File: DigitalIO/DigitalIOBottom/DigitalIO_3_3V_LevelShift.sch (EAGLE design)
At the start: 72 parts, among them IC1 MCP23017SP, IC2 ULN2803A, K5 HF46105, K6 HF46105, K7 HF46105, K8 HF46105, P1 DF11-06-2DSA, Q1 BS170, Q2 BS170, Q5 691131710002, Q6 691131710002, Q7 691131710002, Q8 691131710002, X1 691131710005, X2 691131710004

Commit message: Changed some drills, pads, holes, routes and headers.
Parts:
- removed X3: (no value), pinhead:PINHD-1X5
- added 5V, PQ1, PQ2, PQ3, PQ4: WIREPAD1,6/0,8, wirepad:WIREPAD1,6/0,8
- P1: value DF11-06-2DSA -> DF11-06-2DS; device con-hirose-df11:DF11-06-2DSA -> con-hirose-df11:DF11-06-2DS
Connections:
- net +5V: now also 5V.P; no longer X3.1
- net N$28: now also PQ4.P; no longer X3.5
- net N$30: now also PQ3.P; no longer X3.4
- net N$32: now also PQ2.P; no longer X3.3
- net N$34: now also PQ1.P; no longer X3.2

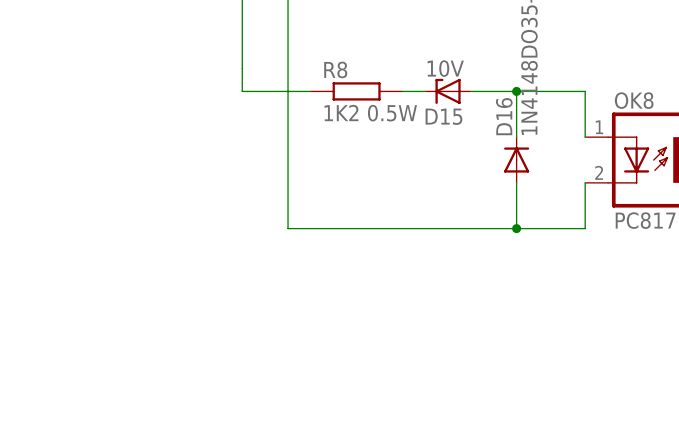
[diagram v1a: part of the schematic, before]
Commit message: Add ground planes. Prepare for production.
Signed-off-by: Alexander Falkenstern <alexander.falkenstern@gmail.com>
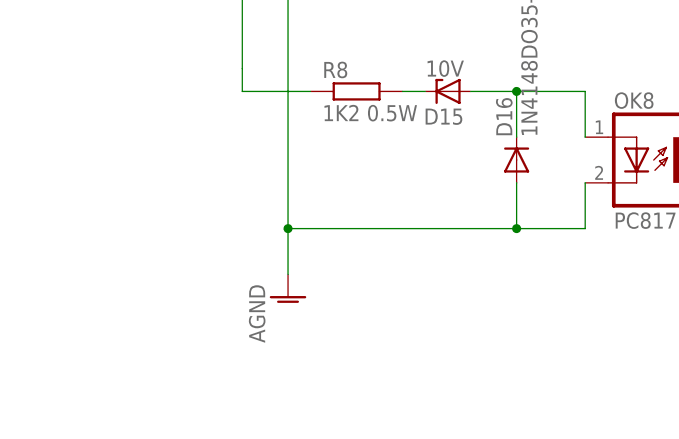
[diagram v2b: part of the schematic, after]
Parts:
- C1, C2: device capacitor-wima:C2,5-3 -> rcl:C-EUC0805
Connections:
- net N$11 renamed AGND

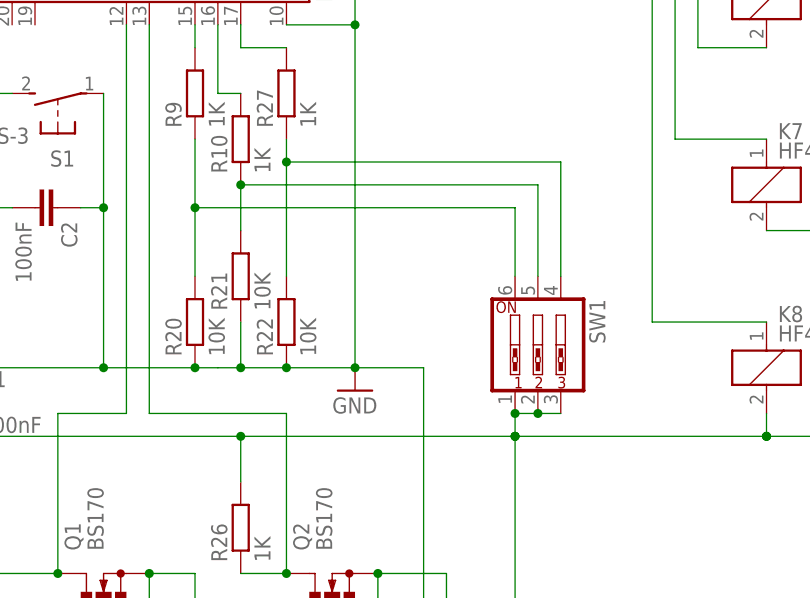
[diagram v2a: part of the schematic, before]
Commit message: Fix address selection. Increase some drills.
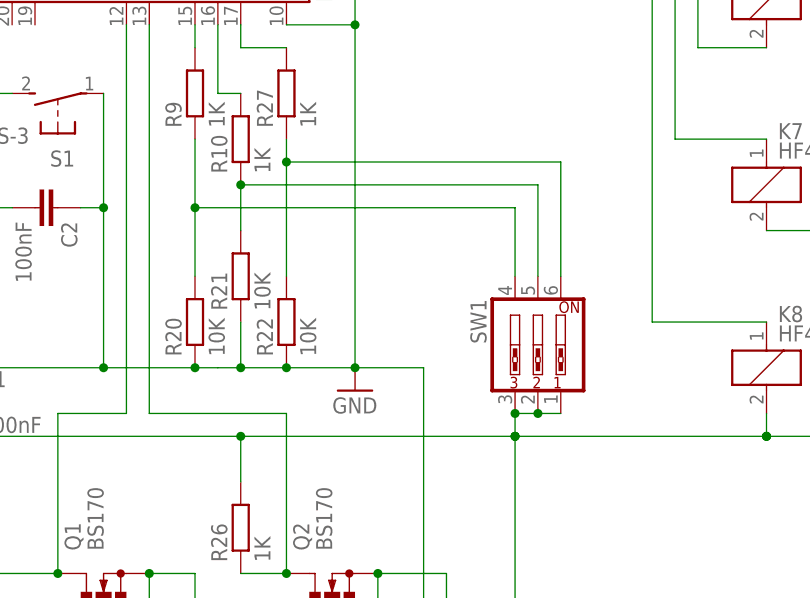
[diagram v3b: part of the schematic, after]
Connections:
- removed net N$36: R22.2, R27.1, SW1.4
- new net N$11: R22.2, R27.1, SW1.6
- net N$77: now also SW1.4; no longer SW1.6
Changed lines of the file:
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@@
 <attribute name="MPN" x="-335.28" y="83.82" size="1.778" layer="96" display="off"/>
 </instance>
-<instance part="SW1" gate="A" x="-271.78" y="76.2" rot="R270">
-<attribute name="OC_FARNELL" x="-271.78" y="76.2" size="1.778" layer="96" display="off"/>
-<attribute name="MF" x="-271.78" y="76.2" size="1.778" layer="96" display="off"/>
-<attribute name="MPN" x="-271.78" y="76.2" size="1.778" layer="96" display="off"/>
+<instance part="SW1" gate="A" x="-271.78" y="76.2" rot="MR270">
+<attribute name="OC_FARNELL" x="-271.78" y="76.2" size="1.778" layer="96" rot="MR0" display="off"/>
+<attribute name="MF" x="-271.78" y="76.2" size="1.778" layer="96" rot="MR0" display="off"/>
+<attribute name="MPN" x="-271.78" y="76.2" size="1.778" layer="96" rot="MR0" display="off"/>
 </instance>
 <instance part="R20" gate="G$1" x="-309.88" y="78.74" rot="R90">
@@
 <junction x="-233.68" y="88.9"/>
 <pinref part="IC1" gate="G$1" pin="VDD"/>
-<pinref part="SW1" gate="A" pin="1"/>
-<pinref part="SW1" gate="A" pin="2"/>
-<pinref part="SW1" gate="A" pin="3"/>
 <wire x1="-340.36" y1="66.04" x2="-340.36" y2="78.74" width="0.1524" layer="91"/>
 <wire x1="-340.36" y1="78.74" x2="-340.36" y2="111.76" width="0.1524" layer="91"/>
-<wire x1="-271.78" y1="68.58" x2="-269.24" y2="68.58" width="0.1524" layer="91"/>
 <pinref part="OK8" gate="A" pin="COL"/>
-<wire x1="-271.78" y1="68.58" x2="-274.32" y2="68.58" width="0.1524" layer="91"/>
 <wire x1="-383.54" y1="43.18" x2="-370.84" y2="43.18" width="0.1524" layer="91"/>
 <wire x1="-370.84" y1="43.18" x2="-370.84" y2="66.04" width="0.1524" layer="91"/>
@@
 <junction x="-340.36" y="78.74"/>
 <wire x1="-274.32" y1="66.04" x2="-304.8" y2="66.04" width="0.1524" layer="91"/>
-<junction x="-274.32" y="68.58"/>
-<wire x1="-274.32" y1="68.58" x2="-274.32" y2="66.04" width="0.1524" layer="91"/>
-<junction x="-271.78" y="68.58"/>
 <wire x1="-340.36" y1="66.04" x2="-335.28" y2="66.04" width="0.1524" layer="91"/>
 <wire x1="-335.28" y1="66.04" x2="-304.8" y2="66.04" width="0.1524" layer="91"/>
@@
 <pinref part="5V" gate="G$1" pin="P"/>
 <junction x="-233.68" y="175.26"/>
+<pinref part="SW1" gate="A" pin="1"/>
+<pinref part="SW1" gate="A" pin="3"/>
+<pinref part="SW1" gate="A" pin="2"/>
+<wire x1="-271.78" y1="68.58" x2="-274.32" y2="68.58" width="0.1524" layer="91"/>
+<junction x="-271.78" y="68.58"/>
+<wire x1="-271.78" y1="68.58" x2="-269.24" y2="68.58" width="0.1524" layer="91"/>
+<wire x1="-274.32" y1="66.04" x2="-274.32" y2="68.58" width="0.1524" layer="91"/>
+<junction x="-274.32" y="68.58"/>
 </segment>
 </net>
@@
 <segment>
 <pinref part="R20" gate="G$1" pin="2"/>
-<wire x1="-309.88" y1="83.82" x2="-309.88" y2="91.44" width="0.1524" layer="91"/>
-<pinref part="SW1" gate="A" pin="6"/>
-<wire x1="-309.88" y1="91.44" x2="-274.32" y2="91.44" width="0.1524" layer="91"/>
-<wire x1="-274.32" y1="91.44" x2="-274.32" y2="83.82" width="0.1524" layer="91"/>
 <pinref part="R9" gate="G$1" pin="1"/>
 <wire x1="-309.88" y1="99.06" x2="-309.88" y2="91.44" width="0.1524" layer="91"/>
+<pinref part="SW1" gate="A" pin="4"/>
+<wire x1="-309.88" y1="91.44" x2="-309.88" y2="83.82" width="0.1524" layer="91"/>
+<wire x1="-274.32" y1="83.82" x2="-274.32" y2="91.44" width="0.1524" layer="91"/>
+<wire x1="-274.32" y1="91.44" x2="-309.88" y2="91.44" width="0.1524" layer="91"/>
 <junction x="-309.88" y="91.44"/>
 </segment>
@@
 <pinref part="R10" gate="G$1" pin="1"/>
 <junction x="-304.8" y="93.98"/>
-</segment>
-</net>
-<net name="N$36" class="0">
-<segment>
-<pinref part="R22" gate="G$1" pin="2"/>
-<wire x1="-299.72" y1="99.06" x2="-299.72" y2="96.52" width="0.1524" layer="91"/>
-<pinref part="R27" gate="G$1" pin="1"/>
-<pinref part="SW1" gate="A" pin="4"/>
-<wire x1="-299.72" y1="96.52" x2="-299.72" y2="83.82" width="0.1524" layer="91"/>
-<wire x1="-269.24" y1="96.52" x2="-269.24" y2="83.82" width="0.1524" layer="91"/>
-<wire x1="-299.72" y1="96.52" x2="-269.24" y2="96.52" width="0.1524" layer="91"/>
-<junction x="-299.72" y="96.52"/>
 </segment>
 </net>
@@
 </segment>
 </net>
+<net name="N$11" class="0">
+<segment>
+<pinref part="SW1" gate="A" pin="6"/>
+<wire x1="-269.24" y1="96.52" x2="-269.24" y2="83.82" width="0.1524" layer="91"/>
+<pinref part="R22" gate="G$1" pin="2"/>
+<pinref part="R27" gate="G$1" pin="1"/>
+<wire x1="-299.72" y1="99.06" x2="-299.72" y2="96.52" width="0.1524" layer="91"/>
+<wire x1="-299.72" y1="96.52" x2="-299.72" y2="83.82" width="0.1524" layer="91"/>
+<wire x1="-269.24" y1="96.52" x2="-299.72" y2="96.52" width="0.1524" layer="91"/>
+<junction x="-299.72" y="96.52"/>
+</segment>
+</net>

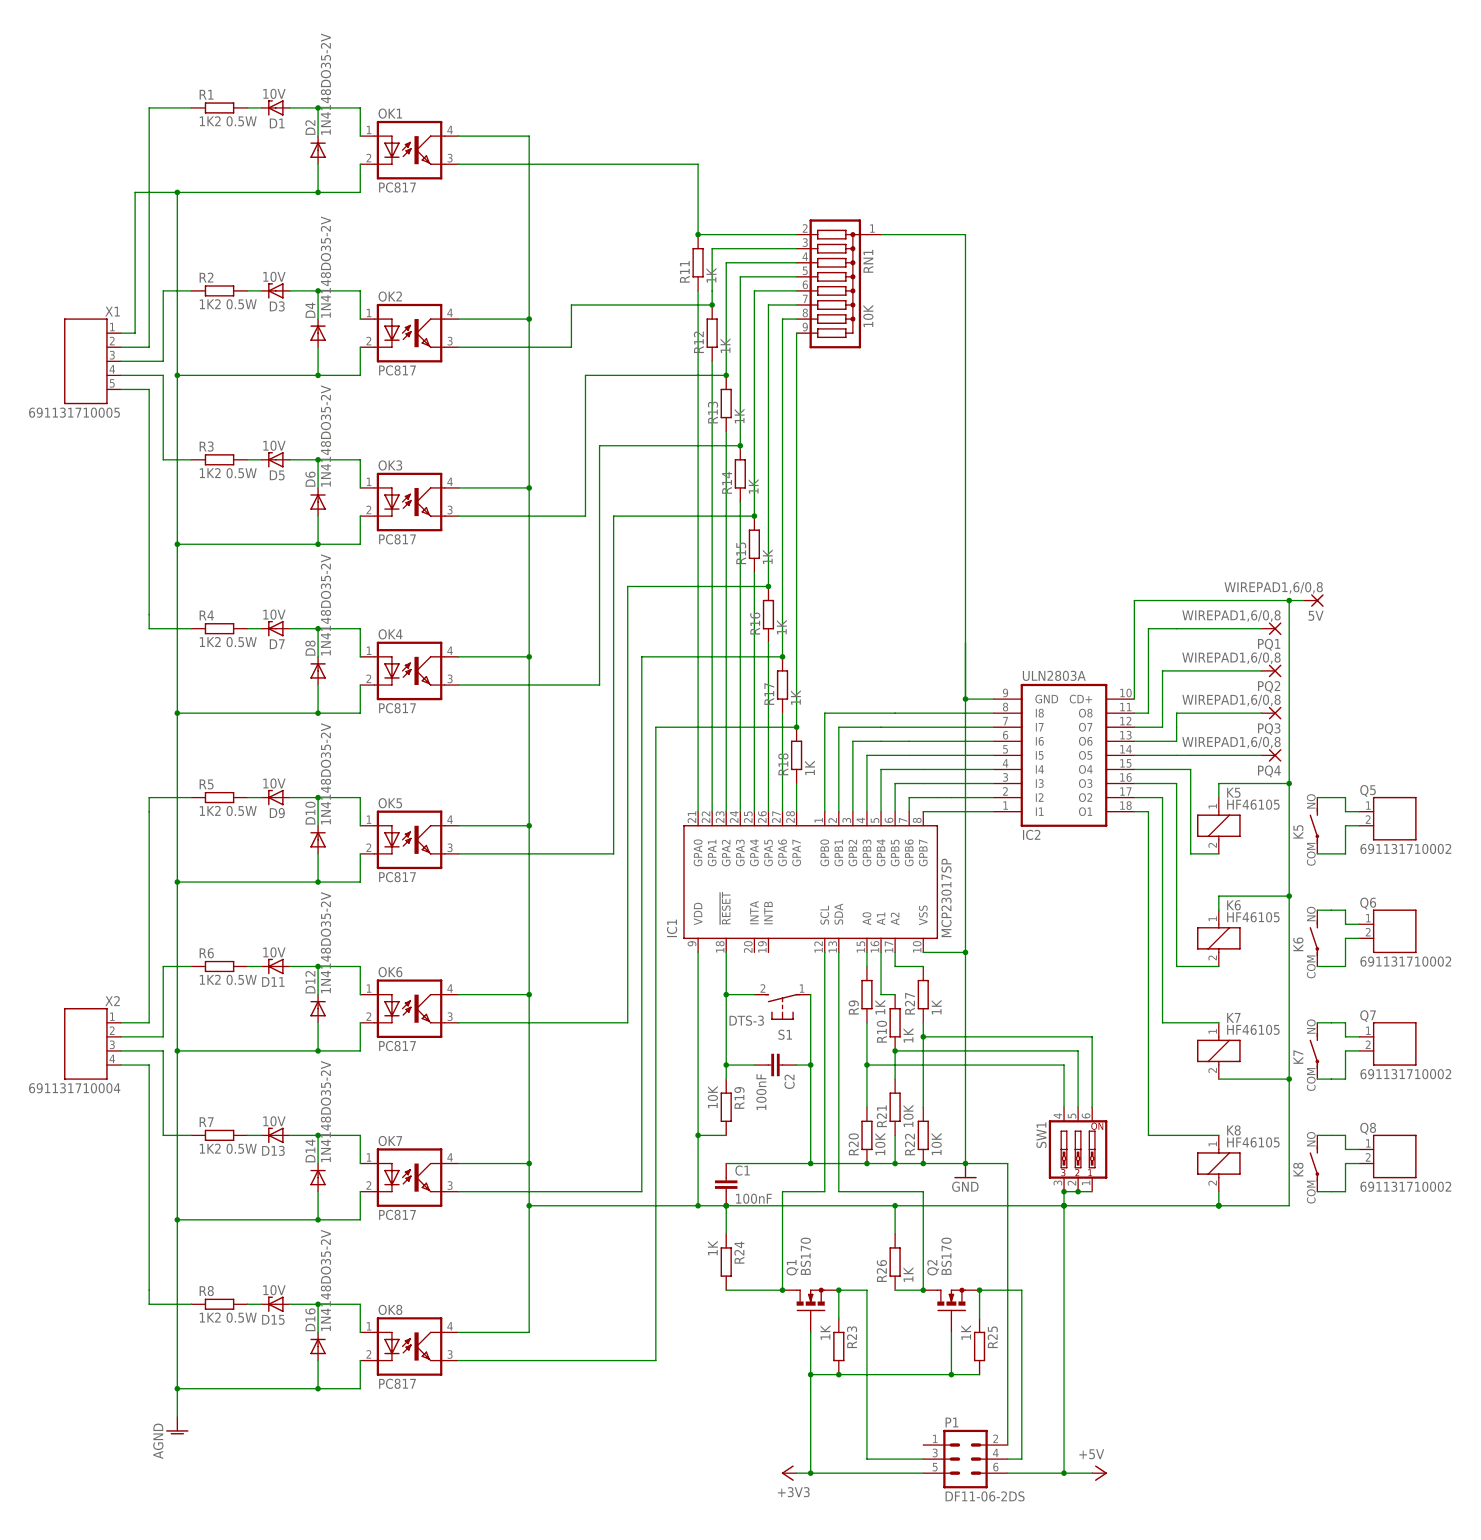
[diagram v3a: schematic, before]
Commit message: Add power switch and I2C interrupt wire. Add pull-up resistors for I2C. Adapt drills.
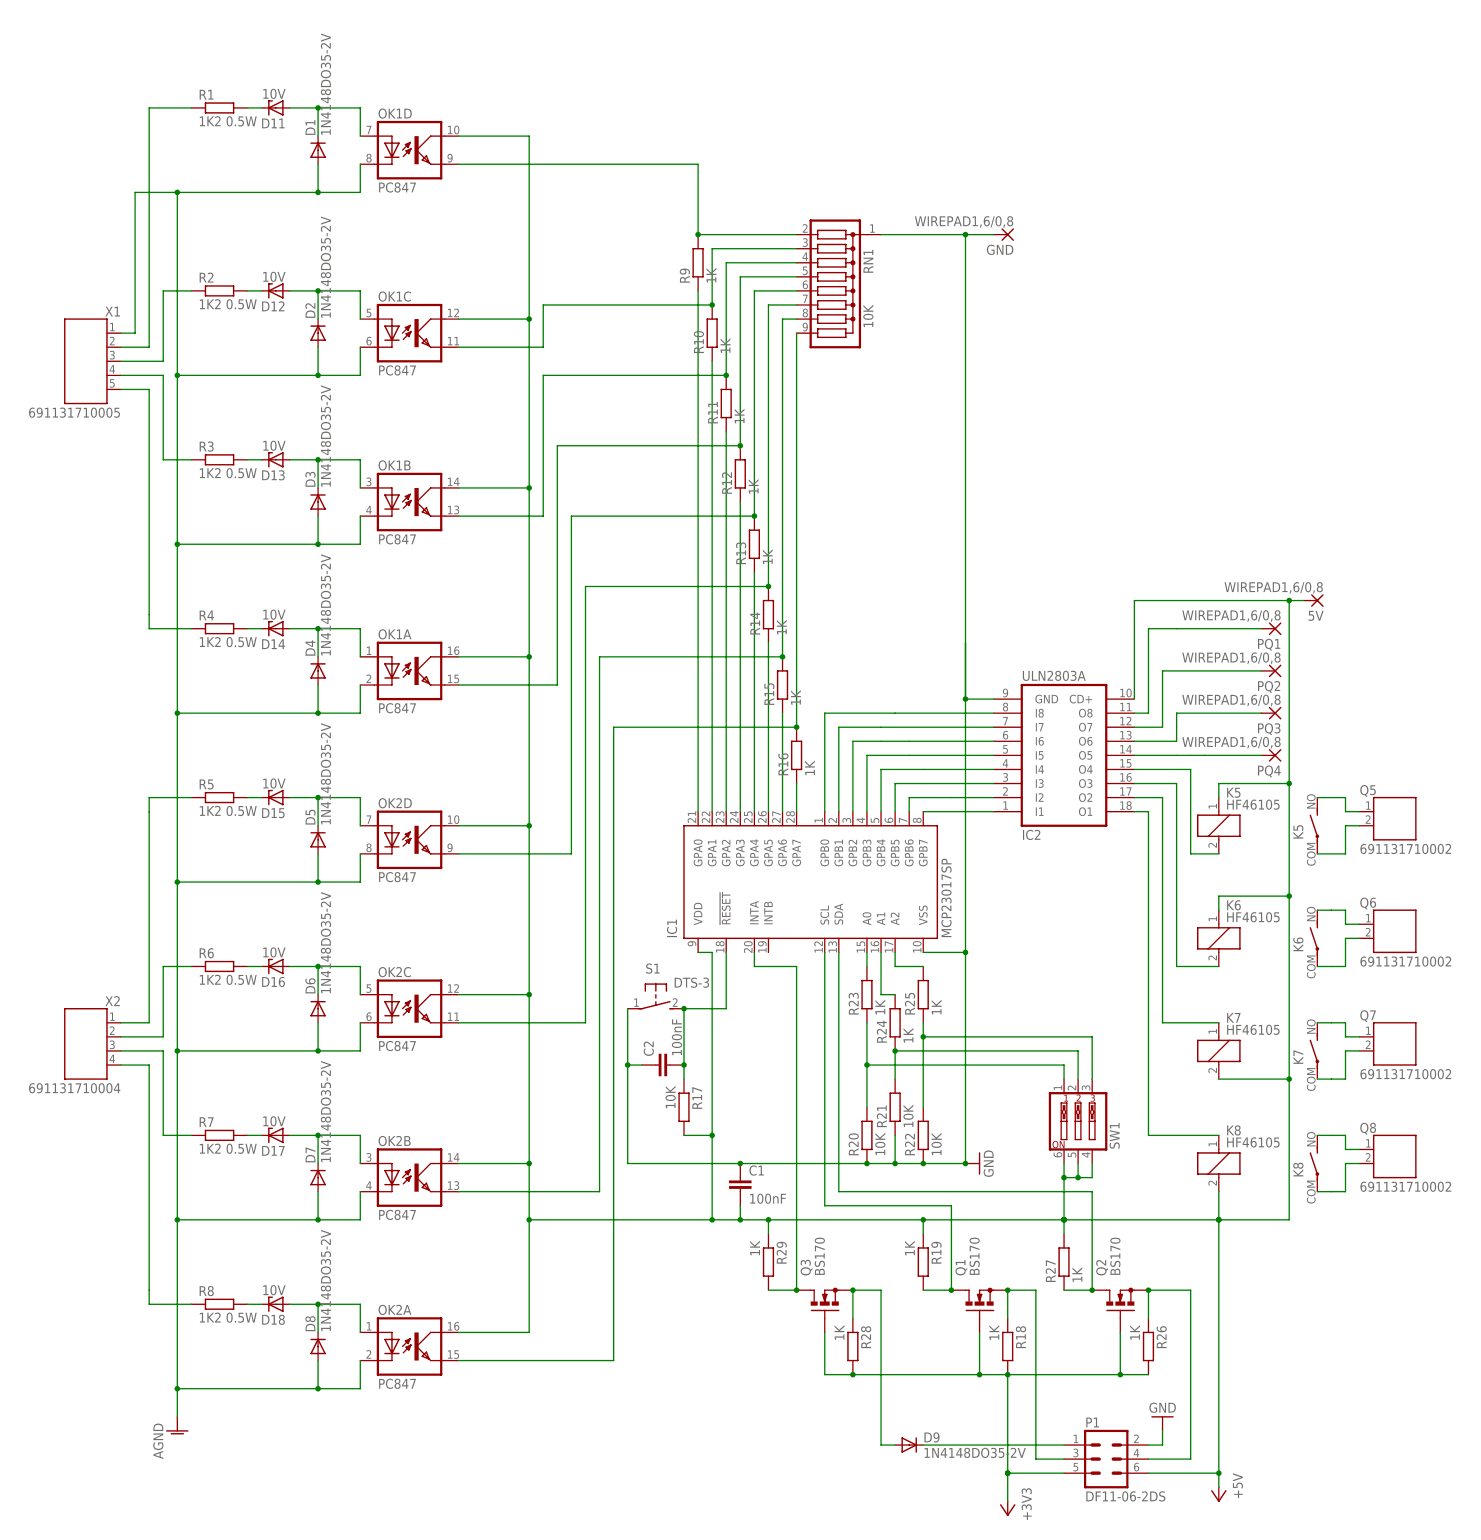
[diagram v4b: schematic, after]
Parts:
- removed D10: 1N4148DO35-2V, diode:1N4148DO35-2V
- removed OK3, OK4, OK5, OK6, OK7, OK8: PC817, optocoupler:PC817
- added D17, D18: 10V, diode:ZENER-DIODEZD-2.5
- added GND: WIREPAD1,6/0,8, wirepad:WIREPAD1,6/0,8
- added Q3: BS170, transistor-small-signal:BS170
- added R28, R29: 1K, rcl:R-EU_0204/2V
- D1, D3, D5, D7, D9: value 10V -> 1N4148DO35-2V; device diode:ZENER-DIODEZD-2.5 -> diode:1N4148DO35-2V
- D12, D14, D16: value 1N4148DO35-2V -> 10V; device diode:1N4148DO35-2V -> diode:ZENER-DIODEZD-2.5
- IC1: device microchip:MCP23017SP -> mcp:MCP23017SP
- OK1, OK2: value PC817 -> PC847; device optocoupler:PC817 -> optocoupler:PC847; MF SHARP -> (none)
- R17: value 1K -> 10K
- R18, R27: device resistor:R-EU_0204/2V -> rcl:R-EU_0204/2V
- R19: value 10K -> 1K; device resistor:R-EU_0204/2V -> rcl:R-EU_0204/2V
- R23, R24, R25: device rcl:R-EU_0204/2V -> resistor:R-EU_0204/2V
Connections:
- new net N$36: D9.A, Q3.S, R28.1
- new net N$80: D9.C, P1.1
- new net N$81: IC1.INTA, Q3.D, R29.2
- net +3V3: now also Q3.G, R18.2, R26.2, R28.2; no longer R23.2, R25.2
- net +5V: now also OK1A.COL, OK1B.COL, OK1C.COL, OK1D.COL, OK2A.COL, OK2B.COL, OK2C.COL, OK2D.COL, R17.2, R19.1, R27.2, R29.1, SW1.4, SW1.5, SW1.6; no longer OK1.COL, OK2.COL, OK3.COL, OK4.COL, OK5.COL, OK6.COL, OK7.COL, OK8.COL, R19.2, R24.1, R26.2, SW1.1, SW1.2, SW1.3
- net AGND: now also D1.A, D3.A, D5.A, D7.A, OK1A.C, OK1B.C, OK1C.C, OK1D.C, OK2A.C, OK2B.C, OK2C.C, OK2D.C; no longer D10.A, D12.A, D14.A, D16.A, OK1.C, OK2.C, OK3.C, OK4.C, OK5.C, OK6.C, OK7.C, OK8.C
- net GND: now also GND.P
- net N$10: now also D11.C; no longer D1.C
- net N$11: now also R25.1, SW1.3; no longer R27.1, SW1.6
- net N$12: now also D1.C, D11.A, OK1D.A; no longer D1.A, D2.C, OK1.A
- net N$15: now also OK1D.EMIT, R9.2; no longer OK1.EMIT, R11.2
- net N$19: now also D12.A, D2.C, OK1C.A; no longer D3.A, D4.C, OK2.A
- net N$20: now also OK1C.EMIT, R10.2; no longer OK2.EMIT, R12.2
- net N$21: now also D13.C; no longer D5.C
- net N$23: now also D13.A, D3.C, OK1B.A; no longer D5.A, D6.C, OK3.A
- net N$25: now also OK1B.EMIT, R11.2; no longer OK3.EMIT, R13.2
- net N$27: now also D14.C; no longer D7.C
- net N$29: now also D14.A, D4.C, OK1A.A; no longer D7.A, D8.C, OK4.A
- net N$31: now also OK1A.EMIT, R12.2; no longer OK4.EMIT, R14.2
- net N$33: now also D15.C; no longer D9.C
- net N$35: now also D15.A, D5.C, OK2D.A; no longer D10.C, D9.A, OK5.A
- net N$37: now also OK2D.EMIT, R13.2; no longer OK5.EMIT, R15.2
- net N$39: now also D16.C; no longer D11.C
- net N$41: now also D16.A, D6.C, OK2C.A; no longer D11.A, D12.C, OK6.A
- net N$43: now also OK2C.EMIT, R14.2; no longer OK6.EMIT, R16.2
- net N$45: now also D17.C; no longer D13.C
- net N$47: now also D17.A, D7.C, OK2B.A; no longer D13.A, D14.C, OK7.A
- net N$49: now also OK2B.EMIT, R15.2; no longer OK7.EMIT, R17.2
- net N$50: now also R23.2; no longer R9.2
- net N$51: now also D18.C; no longer D15.C
- net N$52: now also R24.2; no longer R10.2
- net N$53: now also D18.A, D8.C, OK2A.A; no longer D15.A, D16.C, OK8.A
- net N$55: now also OK2A.EMIT, R16.2; no longer OK8.EMIT, R18.2
- net N$57: now also R17.1; no longer R19.1
- net N$58: now also R19.2; no longer R24.2
- net N$59: now also R9.1; no longer R11.1
- net N$60: now also R10.1; no longer R12.1
- net N$61: now also R27.1; no longer R26.1
- net N$62: now also R11.1; no longer R13.1
- net N$63: now also R16.1; no longer R18.1
- net N$64: now also R15.1; no longer R17.1
- net N$65: now also R14.1; no longer R16.1
- net N$67: now also R13.1; no longer R15.1
- net N$68: now also R12.1; no longer R14.1
- net N$69: now also R26.1; no longer R25.1
- net N$71: now also R18.1; no longer R23.1
- net N$77: now also R23.1, SW1.1; no longer R9.1, SW1.4
- net N$78: now also R24.1, SW1.2; no longer R10.1, SW1.5
- net N$79: now also R25.2; no longer R27.2
- net N$9: now also D12.C; no longer D3.C
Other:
- moved on the sheet: C1, C2, D11, D13, D15, D2, D4, D6, D8, OK1A, OK2A, P1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
